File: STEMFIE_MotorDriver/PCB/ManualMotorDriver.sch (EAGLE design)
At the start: 16 parts, among them U1 STM32F030F4P6, U2 LP2985-33DBVR, U3 L9110SO8, X1 53048-05

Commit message: Update Library
Created custom library for parts not in the standard Eagle libraries.
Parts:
- U1: device STM32:STM32F030F4P6 -> STEMFIE_Electrics:STM32F030F4P6
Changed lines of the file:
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@@
 </classes>
 <parts>
-<part name="U1" library="STM32" deviceset="STM32F030F4P6" device=""/>
+<part name="U1" library="STEMFIE_Electrics" deviceset="STM32F030F4P6" device="" package3d_urn="urn:adsk.eagle:package:4349/3"/>
 <part name="U2" library="LP2985-33DBVR" deviceset="LP2985-33DBVR" device=""/>
 <part name="U3" library="L9110" deviceset="L9110" device="SO8"/>

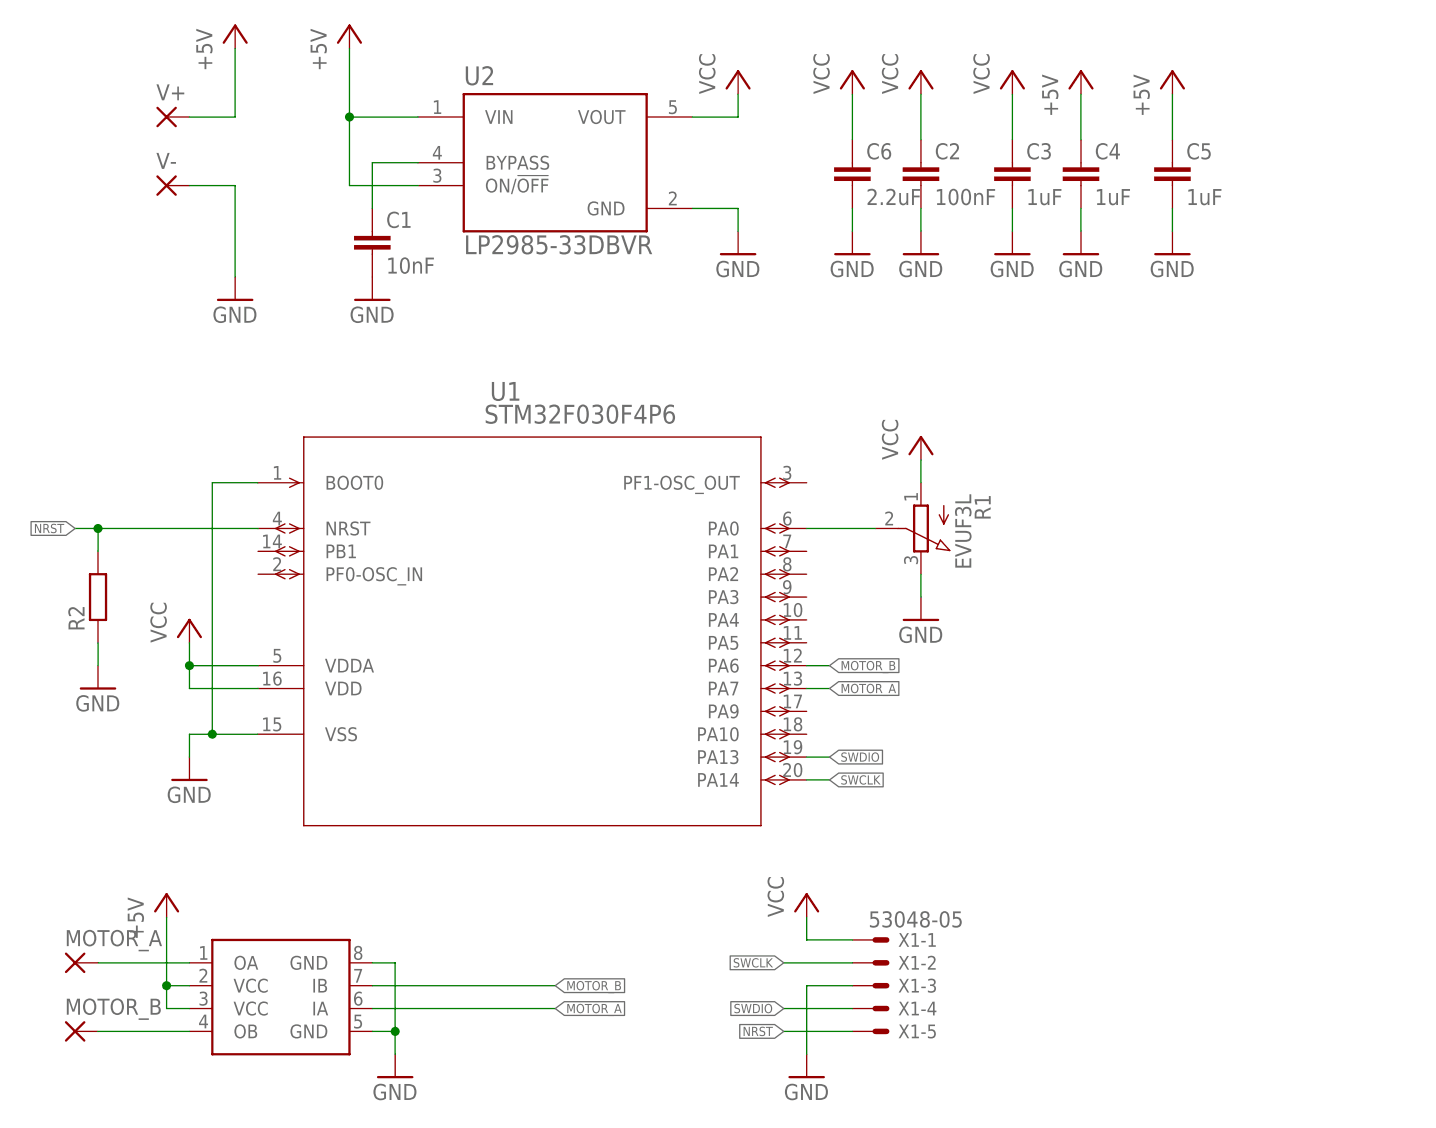
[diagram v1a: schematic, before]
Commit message: Fixed NRST
nRST was pulled down instead of up. Yeah ...
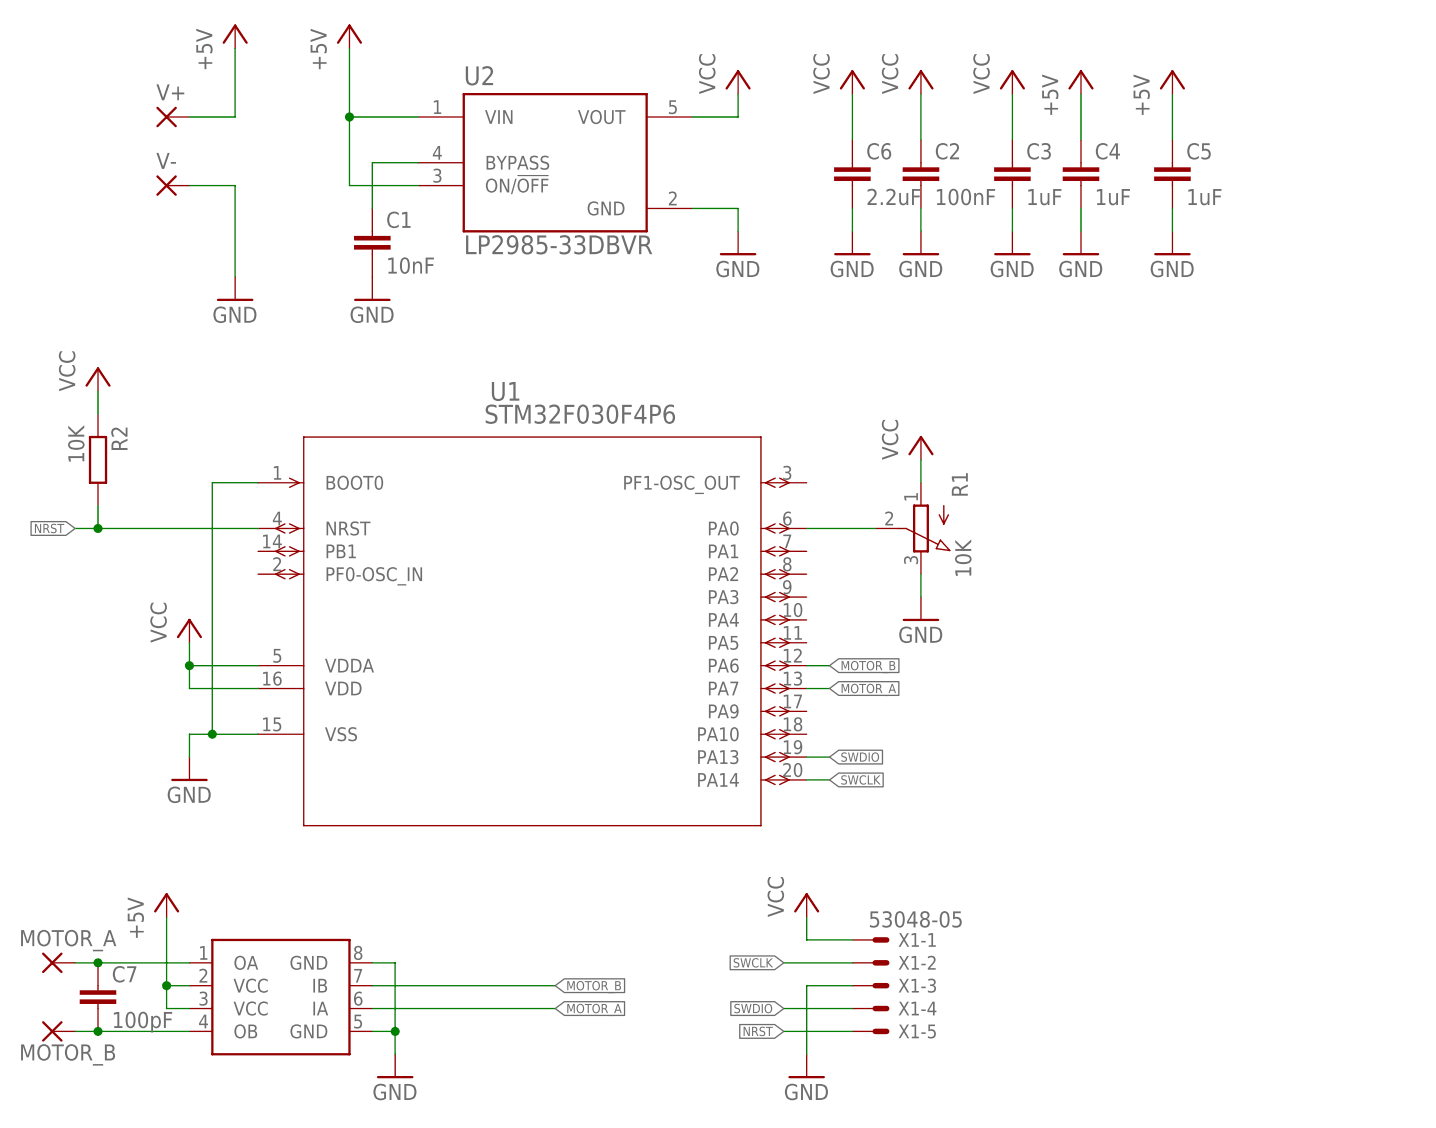
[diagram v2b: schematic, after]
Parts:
- added C7: 100pF, rcl:C-EUC0805
- R1: value EVUF3L -> 10K
- R2: value (none) -> 10K
- U2: device LP2985-33DBVR:LP2985-33DBVR -> STEMFIE_Electrics:LP2985-33DBVR
- U3: device L9110:L9110SO8 -> STEMFIE_Electrics:L9110SO8
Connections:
- net GND: no longer R2.1
- net N$4: now also C7.1
- net N$5: now also C7.2
- net VCC: now also R2.1
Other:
- moved on the sheet: MOTOR_A, MOTOR_B, R2
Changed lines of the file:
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@@
 <parts>
 <part name="U1" library="STEMFIE_Electrics" deviceset="STM32F030F4P6" device="" package3d_urn="urn:adsk.eagle:package:4349/3"/>
-<part name="U2" library="LP2985-33DBVR" deviceset="LP2985-33DBVR" device=""/>
-<part name="U3" library="L9110" deviceset="L9110" device="SO8"/>
+<part name="U2" library="STEMFIE_Electrics" deviceset="LP2985-33DBVR" device="" package3d_urn="urn:adsk.eagle:package:16378354/2"/>
+<part name="U3" library="STEMFIE_Electrics" deviceset="L9110" device="SO8" package3d_urn="urn:adsk.eagle:package:7566865/2"/>
 <part name="P+1" library="supply1" library_urn="urn:adsk.eagle:library:371" deviceset="VCC" device=""/>
 <part name="GND1" library="supply1" library_urn="urn:adsk.eagle:library:371" deviceset="GND" device=""/>
@@
 <part name="P+4" library="supply1" library_urn="urn:adsk.eagle:library:371" deviceset="+5V" device=""/>
 <part name="GND3" library="supply1" library_urn="urn:adsk.eagle:library:371" deviceset="GND" device=""/>
-<part name="R2" library="rcl" library_urn="urn:adsk.eagle:library:334" deviceset="R-EU_" device="R0402" package3d_urn="urn:adsk.eagle:package:23547/3"/>
-<part name="GND4" library="supply1" library_urn="urn:adsk.eagle:library:371" deviceset="GND" device=""/>
+<part name="R2" library="rcl" library_urn="urn:adsk.eagle:library:334" deviceset="R-EU_" device="R0402" package3d_urn="urn:adsk.eagle:package:23547/3" value="10K"/>
 <part name="GND5" library="supply1" library_urn="urn:adsk.eagle:library:371" deviceset="GND" device=""/>
 <part name="MOTOR_A" library="wirepad" library_urn="urn:adsk.eagle:library:412" deviceset="WIREPAD" device="SMD2,54-5,08" package3d_urn="urn:adsk.eagle:package:30841/1" value=""/>
@@
 <part name="X1" library="con-molex" library_urn="urn:adsk.eagle:library:165" deviceset="53?-05" device="048" package3d_urn="urn:adsk.eagle:package:8078563/1"/>
 <part name="P+5" library="supply1" library_urn="urn:adsk.eagle:library:371" deviceset="+5V" device=""/>
-<part name="R1" library="pot" library_urn="urn:adsk.eagle:library:331" deviceset="EVU" device="L" package3d_urn="urn:adsk.eagle:package:22736/1" technology="F3"/>
+<part name="R1" library="pot" library_urn="urn:adsk.eagle:library:331" deviceset="EVU" device="L" package3d_urn="urn:adsk.eagle:package:22736/1" technology="F3" value="10K"/>
 <part name="GND8" library="supply1" library_urn="urn:adsk.eagle:library:371" deviceset="GND" device=""/>
 <part name="P+7" library="supply1" library_urn="urn:adsk.eagle:library:371" deviceset="VCC" device=""/>
@@
 <part name="GND13" library="supply1" library_urn="urn:adsk.eagle:library:371" deviceset="GND" device=""/>
 <part name="C6" library="rcl" library_urn="urn:adsk.eagle:library:334" deviceset="C-EU" device="C0805" package3d_urn="urn:adsk.eagle:package:23617/2" value="2.2uF"/>
+<part name="C7" library="rcl" library_urn="urn:adsk.eagle:library:334" deviceset="C-EU" device="C0805" package3d_urn="urn:adsk.eagle:package:23617/2" value="100pF"/>
+<part name="P+13" library="supply1" library_urn="urn:adsk.eagle:library:371" deviceset="VCC" device=""/>
 </parts>
 <sheets>
@@
 <attribute name="VALUE" x="91.44" y="91.44" size="1.778" layer="96"/>
 </instance>
-<instance part="R2" gate="G$1" x="22.86" y="55.88" smashed="yes" rot="R90">
-<attribute name="NAME" x="21.3614" y="52.07" size="1.778" layer="95" rot="R90"/>
-<attribute name="VALUE" x="26.162" y="52.07" size="1.778" layer="96" rot="R90"/>
-</instance>
-<instance part="GND4" gate="1" x="22.86" y="45.72" smashed="yes">
-<attribute name="VALUE" x="20.32" y="43.18" size="1.778" layer="96"/>
+<instance part="R2" gate="G$1" x="22.86" y="71.12" smashed="yes" rot="R270">
+<attribute name="NAME" x="24.3586" y="74.93" size="1.778" layer="95" rot="R270"/>
+<attribute name="VALUE" x="19.558" y="74.93" size="1.778" layer="96" rot="R270"/>
 </instance>
 <instance part="GND5" gate="1" x="55.88" y="2.54" smashed="yes">
 <attribute name="VALUE" x="53.34" y="0" size="1.778" layer="96"/>
 </instance>
-<instance part="MOTOR_A" gate="G$1" x="20.32" y="15.24" smashed="yes">
-<attribute name="NAME" x="19.177" y="17.0942" size="1.778" layer="95"/>
-<attribute name="VALUE" x="19.177" y="11.938" size="1.778" layer="96"/>
-</instance>
-<instance part="MOTOR_B" gate="G$1" x="20.32" y="7.62" smashed="yes">
-<attribute name="NAME" x="19.177" y="9.4742" size="1.778" layer="95"/>
-<attribute name="VALUE" x="19.177" y="4.318" size="1.778" layer="96"/>
+<instance part="MOTOR_A" gate="G$1" x="17.78" y="15.24" smashed="yes">
+<attribute name="NAME" x="14.097" y="17.0942" size="1.778" layer="95"/>
+<attribute name="VALUE" x="16.637" y="11.938" size="1.778" layer="96"/>
+</instance>
+<instance part="MOTOR_B" gate="G$1" x="17.78" y="7.62" smashed="yes">
+<attribute name="NAME" x="14.097" y="4.3942" size="1.778" layer="95"/>
+<attribute name="VALUE" x="16.637" y="4.318" size="1.778" layer="96"/>
 </instance>
 <instance part="V+" gate="G$1" x="30.48" y="109.22" smashed="yes">
@@
 </instance>
 <instance part="R1" gate="G$1" x="114.3" y="63.5" smashed="yes" rot="R180">
-<attribute name="NAME" x="120.269" y="67.31" size="1.778" layer="95" rot="R270"/>
-<attribute name="VALUE" x="118.11" y="67.31" size="1.778" layer="96" rot="R270"/>
+<attribute name="NAME" x="117.729" y="69.85" size="1.778" layer="95" rot="R270"/>
+<attribute name="VALUE" x="118.11" y="62.23" size="1.778" layer="96" rot="R270"/>
 </instance>
 <instance part="GND8" gate="1" x="101.6" y="2.54" smashed="yes">
@@
 <attribute name="NAME" x="108.204" y="104.521" size="1.778" layer="95"/>
 <attribute name="VALUE" x="108.204" y="99.441" size="1.778" layer="96"/>
+</instance>
+<instance part="C7" gate="G$1" x="22.86" y="12.7" smashed="yes">
+<attribute name="NAME" x="24.384" y="13.081" size="1.778" layer="95"/>
+<attribute name="VALUE" x="24.384" y="8.001" size="1.778" layer="96"/>
+</instance>
+<instance part="P+13" gate="VCC" x="22.86" y="81.28" smashed="yes">
+<attribute name="VALUE" x="20.32" y="78.74" size="1.778" layer="96" rot="R90"/>
 </instance>
 </instances>
@@
 <pinref part="C6" gate="G$1" pin="1"/>
 <wire x1="106.68" y1="106.68" x2="106.68" y2="111.76" width="0.1524" layer="91"/>
+</segment>
+<segment>
+<pinref part="R2" gate="G$1" pin="1"/>
+<wire x1="22.86" y1="76.2" x2="22.86" y2="78.74" width="0.1524" layer="91"/>
+<pinref part="P+13" gate="VCC" pin="VCC"/>
 </segment>
 </net>
@@
 </segment>
 <segment>
-<pinref part="R2" gate="G$1" pin="1"/>
-<pinref part="GND4" gate="1" pin="GND"/>
-<wire x1="22.86" y1="50.8" x2="22.86" y2="48.26" width="0.1524" layer="91"/>
-</segment>
-<segment>
 <pinref part="U3" gate="G$1" pin="GND@1"/>
 <wire x1="53.34" y1="15.24" x2="55.88" y2="15.24" width="0.1524" layer="91"/>
@@
 <wire x1="40.64" y1="63.5" x2="22.86" y2="63.5" width="0.1524" layer="91"/>
 <pinref part="R2" gate="G$1" pin="2"/>
-<wire x1="22.86" y1="60.96" x2="22.86" y2="63.5" width="0.1524" layer="91"/>
+<wire x1="22.86" y1="66.04" x2="22.86" y2="63.5" width="0.1524" layer="91"/>
 <wire x1="22.86" y1="63.5" x2="20.32" y2="63.5" width="0.1524" layer="91"/>
 <junction x="22.86" y="63.5"/>
@@
 <wire x1="33.02" y1="15.24" x2="22.86" y2="15.24" width="0.1524" layer="91"/>
 <pinref part="MOTOR_A" gate="G$1" pin="P"/>
+<pinref part="C7" gate="G$1" pin="1"/>
+<wire x1="22.86" y1="15.24" x2="20.32" y2="15.24" width="0.1524" layer="91"/>
+<junction x="22.86" y="15.24"/>
 </segment>
 </net>
@@
 <wire x1="33.02" y1="7.62" x2="22.86" y2="7.62" width="0.1524" layer="91"/>
 <pinref part="MOTOR_B" gate="G$1" pin="P"/>
-</segment>
-</net>
+<pinref part="C7" gate="G$1" pin="2"/>
+<wire x1="22.86" y1="7.62" x2="20.32" y2="7.62" width="0.1524" layer="91"/>
+<junction x="22.86" y="7.62"/>
+</segment>
+</net>

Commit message: Added LEDs and reduced size of wire pads
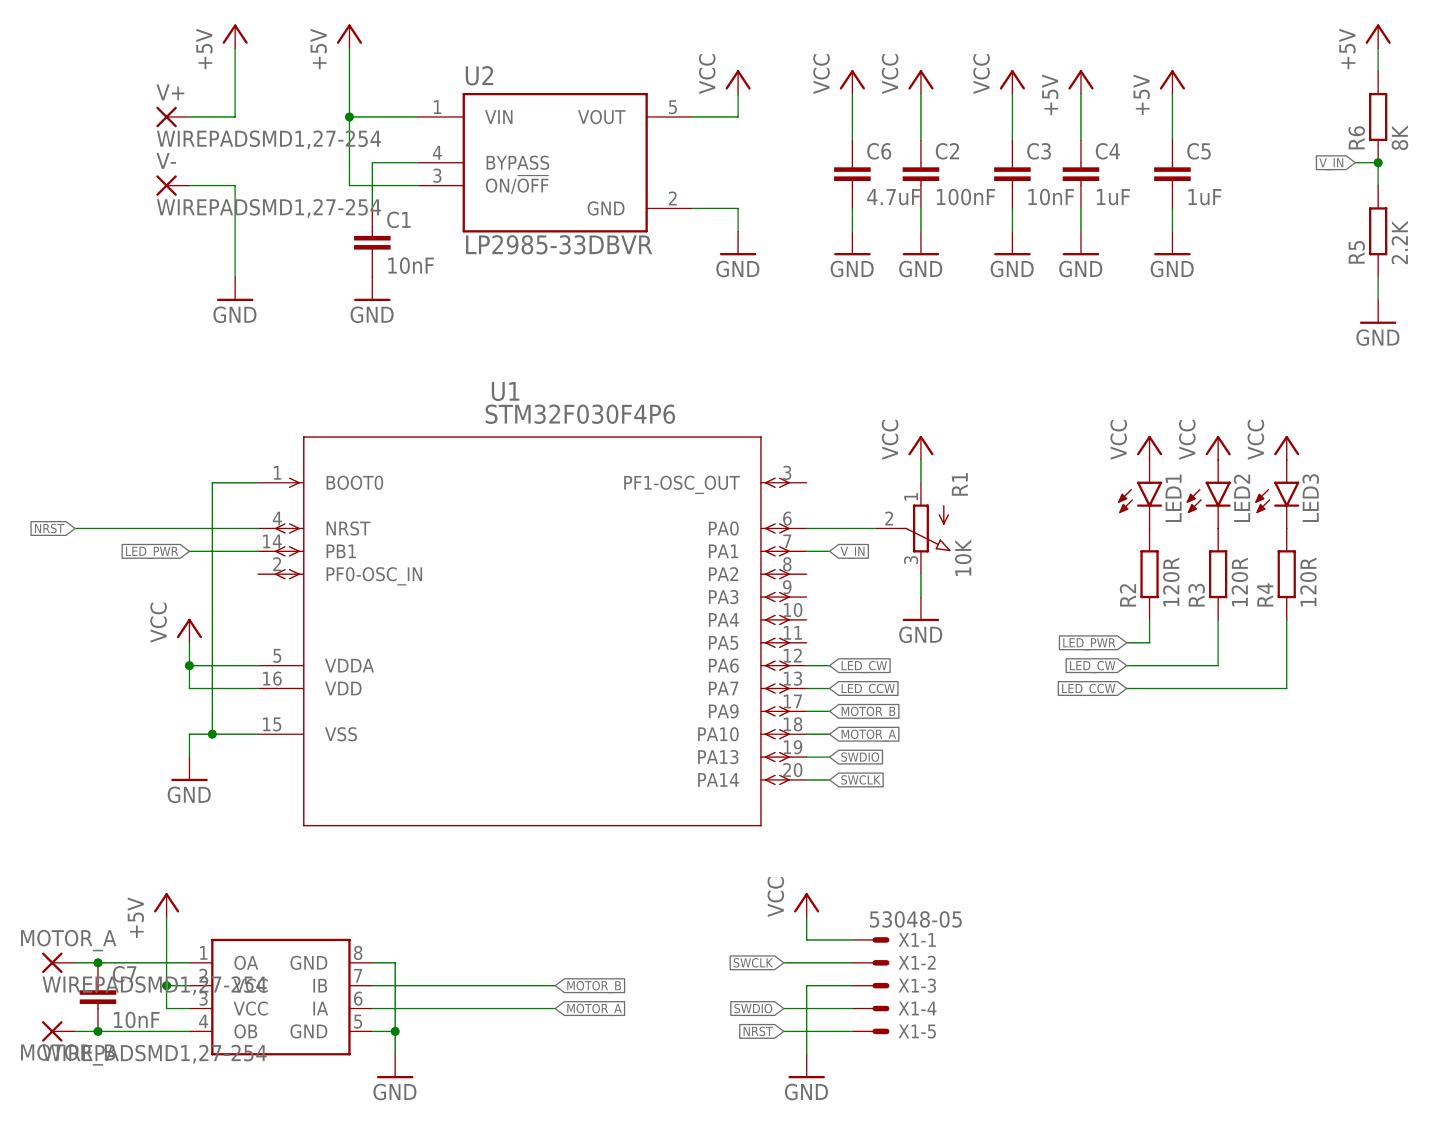
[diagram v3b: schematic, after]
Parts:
- added LED1, LED2, LED3: (no value), led:LEDCHIP-LED0603
- added R3, R4: 120R, rcl:R-EU_R0402
- added R5: 2.2K, rcl:R-EU_R0402
- added R6: 8K, rcl:R-EU_R0402
- C3: value 1uF -> 10nF
- C6: value 2.2uF -> 4.7uF
- C7: value 100pF -> 10nF
- MOTOR_A, MOTOR_B, V+, V-: value WIREPADSMD2,54-5,08 -> WIREPADSMD1,27-254; device wirepad:WIREPADSMD2,54-5,08 -> wirepad:WIREPADSMD1,27-254
- R2: value 10K -> 120R
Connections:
- new net LED_CCW: R4.1, U1.PA7
- new net LED_CW: R3.1, U1.PA6
- new net LED_PWR: R2.1, U1.PB1
- new net N$2: LED1.C, R2.2
- new net N$6: LED2.C, R3.2
- new net N$7: LED3.C, R4.2
- new net V_IN: R5.2, R6.1, U1.PA1
- net +5V: now also R6.2
- net GND: now also R5.1
- net MOTOR_A: now also U1.PA10; no longer U1.PA7
- net MOTOR_B: now also U1.PA9; no longer U1.PA6
- net NRST: no longer R2.2
- net VCC: now also LED1.A, LED2.A, LED3.A; no longer R2.1
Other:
- moved on the sheet: R2
